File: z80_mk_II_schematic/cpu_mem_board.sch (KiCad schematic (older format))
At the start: 23 parts

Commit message: Lots more work on schematic
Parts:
- added C1, C3, C4: 0u1, symbol Device:C_Small
- added C2: 100u, symbol Device:CP_Small
- added J1: Conn_01x37_Male, symbol Connector:Conn_01x37_Male
- gave numbers to parts that had none: 23
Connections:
- net labels added: A0, A1, A10, A11, A12, A13, A2, A3, A4, A5, A6, A7, A8, A9, A[15..0], CPU_CLK, D0, D1, D2, D3, D4, D5, D6, D7, D[7..0], IO_CLK, IO_CLK_IN, NC, ~BUSAK~, ~BUSRQ~, ~EPROM_CE~, ~EXT_RESET~, ~INT~, ~IORQ~, ~M1~, ~MON_WR~, ~MREQ~, ~RAM0_CE~, ~RAM1_CE~, ~RD~, ~RESET_IN~, ~RESET~, ~WR~
- net labels removed: ~BUSAK, ~BUSRQ, ~CPU_CLK, ~CS_EPROM, ~CS_RAM0, ~CS_RAM1, ~INT, ~MON_WR, ~MREQ, ~RD, ~RESET
- wire segments 115 -> 251
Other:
- moved on the sheet: C5, D1, D2, Q1, Q2, Q3, R1, R10, R11, R2, R3, R4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

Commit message: Un-fsck something which made most of the chips into 74LS00 for some very odd reason. Also start to assign footprints.
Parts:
- R1, R10, R11, R2, R3, R4, R5, R6, R7, R8, R9: footprint (none) -> Resistors_ThroughHole:R_Axial_DIN0207_L6.3mm_D2.5mm_P10.16mm_Horizontal
- U1: footprint (none) -> Housings_DIP:DIP-40_W15.24mm_Socket
- U2, U3, U4: footprint Package_DIP:DIP-28_W15.24mm -> Housings_DIP:DIP-28_W15.24mm_Socket
- U5: footprint (none) -> Housings_DIP:DIP-16_W7.62mm_Socket
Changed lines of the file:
@@
 F 0 "R2" V 2300 1550 50  0000 C CNN
 F 1 "4K7" V 2100 1550 50  0000 C CNN
-F 2 "" H 2200 1550 50  0001 C CNN
+F 2 "Resistors_ThroughHole:R_Axial_DIN0207_L6.3mm_D2.5mm_P10.16mm_Horizontal" H 2200 1550 50  0001 C CNN
 F 3 "~" H 2200 1550 50  0001 C CNN
 	1    2200 1550
@@
 F 0 "R1" V 2100 1400 50  0000 C CNN
 F 1 "4K7" V 1900 1400 50  0000 C CNN
-F 2 "" H 2000 1400 50  0001 C CNN
+F 2 "Resistors_ThroughHole:R_Axial_DIN0207_L6.3mm_D2.5mm_P10.16mm_Horizontal" H 2000 1400 50  0001 C CNN
 F 3 "~" H 2000 1400 50  0001 C CNN
 	1    2000 1400
@@
 F 0 "R9" H 7509 5246 50  0000 L CNN
 F 1 "10K" H 7509 5155 50  0000 L CNN
-F 2 "" H 7450 5200 50  0001 C CNN
+F 2 "Resistors_ThroughHole:R_Axial_DIN0207_L6.3mm_D2.5mm_P10.16mm_Horizontal" H 7450 5200 50  0001 C CNN
 F 3 "~" H 7450 5200 50  0001 C CNN
 	1    7450 5200
@@
 F 0 "R8" V 7296 5450 50  0000 C CNN
 F 1 "10K" V 7205 5450 50  0000 C CNN
-F 2 "" H 7100 5450 50  0001 C CNN
+F 2 "Resistors_ThroughHole:R_Axial_DIN0207_L6.3mm_D2.5mm_P10.16mm_Horizontal" H 7100 5450 50  0001 C CNN
 F 3 "~" H 7100 5450 50  0001 C CNN
 	1    7100 5450
@@
 F 0 "R7" H 6841 4754 50  0000 R CNN
 F 1 "4K7" H 6841 4845 50  0000 R CNN
-F 2 "" H 6900 4800 50  0001 C CNN
+F 2 "Resistors_ThroughHole:R_Axial_DIN0207_L6.3mm_D2.5mm_P10.16mm_Horizontal" H 6900 4800 50  0001 C CNN
 F 3 "~" H 6900 4800 50  0001 C CNN
 	1    6900 4800
@@
 F 0 "R6" H 6491 4754 50  0000 R CNN
 F 1 "4K7" H 6491 4845 50  0000 R CNN
-F 2 "" H 6550 4800 50  0001 C CNN
+F 2 "Resistors_ThroughHole:R_Axial_DIN0207_L6.3mm_D2.5mm_P10.16mm_Horizontal" H 6550 4800 50  0001 C CNN
 F 3 "~" H 6550 4800 50  0001 C CNN
 	1    6550 4800
@@
 F 0 "R4" H 5742 1354 50  0000 R CNN
 F 1 "4K7" H 5742 1445 50  0000 R CNN
-F 2 "" H 5800 1400 50  0001 C CNN
+F 2 "Resistors_ThroughHole:R_Axial_DIN0207_L6.3mm_D2.5mm_P10.16mm_Horizontal" H 5800 1400 50  0001 C CNN
 F 3 "~" H 5800 1400 50  0001 C CNN
 	1    5800 1400
@@
 F 0 "U4" H 9050 2500 50  0000 C CNN
 F 1 "KM62256CLP" H 9050 2350 50  0000 C CNN
-F 2 "Package_DIP:DIP-28_W15.24mm" H 9050 2300 50  0001 C CNN
+F 2 "Housings_DIP:DIP-28_W15.24mm_Socket" H 9050 2300 50  0001 C CNN
 F 3 "https://www.futurlec.com/Datasheet/Memory/62256.pdf" H 9050 2300 50  0001 C CNN
 	1    9050 2400
@@
 F 0 "U3" H 7350 2500 50  0000 C CNN
 F 1 "27128" H 7350 2400 50  0000 C CNN
-F 2 "Package_DIP:DIP-28_W15.24mm" H 7300 2600 50  0001 C CNN
+F 2 "Housings_DIP:DIP-28_W15.24mm_Socket" H 7300 2600 50  0001 C CNN
 F 3 "http://eeshop.unl.edu/pdf/27128.pdf" H 7300 2600 50  0001 C CNN
 	1    7300 2600
@@
 F 0 "U2" H 5200 2450 50  0000 C CNN
 F 1 "KM62256CLP" H 5250 2300 50  0000 C CNN
-F 2 "Package_DIP:DIP-28_W15.24mm" H 5200 2300 50  0001 C CNN
+F 2 "Housings_DIP:DIP-28_W15.24mm_Socket" H 5200 2300 50  0001 C CNN
 F 3 "https://www.futurlec.com/Datasheet/Memory/62256.pdf" H 5200 2300 50  0001 C CNN
 	1    5200 2400
@@
 F 0 "U1" H 3050 3050 50  0000 C CNN
 F 1 "Z80CPU" H 3050 2850 50  0000 C CNN
-F 2 "" H 3050 3350 50  0001 C CNN
+F 2 "Housings_DIP:DIP-40_W15.24mm_Socket" H 3050 3350 50  0001 C CNN
 F 3 "www.zilog.com/manage_directlink.php?filepath=docs/z80/um0080" H 3050 3350 50  0001 C CNN
 	1    3050 2950
@@
 F 0 "R10" H 10209 4446 50  0000 L CNN
 F 1 "4K7" H 10209 4355 50  0000 L CNN
-F 2 "" H 10150 4400 50  0001 C CNN
+F 2 "Resistors_ThroughHole:R_Axial_DIN0207_L6.3mm_D2.5mm_P10.16mm_Horizontal" H 10150 4400 50  0001 C CNN
 F 3 "~" H 10150 4400 50  0001 C CNN
 	1    10150 4400
@@
 F 0 "R11" H 10459 4446 50  0000 L CNN
 F 1 "4K7" H 10459 4355 50  0000 L CNN
-F 2 "" H 10400 4400 50  0001 C CNN
+F 2 "Resistors_ThroughHole:R_Axial_DIN0207_L6.3mm_D2.5mm_P10.16mm_Horizontal" H 10400 4400 50  0001 C CNN
 F 3 "~" H 10400 4400 50  0001 C CNN
 	1    10400 4400
@@
 F 0 "U5" H 9250 5300 50  0000 C CNN
 F 1 "74LS156" H 9300 5150 50  0000 C CNN
-F 2 "" H 9250 5150 50  0001 C CNN
+F 2 "Housings_DIP:DIP-16_W7.62mm_Socket" H 9250 5150 50  0001 C CNN
 F 3 "http://www.ti.com/lit/gpn/sn74LS156" H 9250 5150 50  0001 C CNN
 	1    9250 5150
@@
 F 0 "R5" H 6191 2054 50  0000 R CNN
 F 1 "4K7" H 6191 2145 50  0000 R CNN
-F 2 "" H 6250 2100 50  0001 C CNN
+F 2 "Resistors_ThroughHole:R_Axial_DIN0207_L6.3mm_D2.5mm_P10.16mm_Horizontal" H 6250 2100 50  0001 C CNN
 F 3 "~" H 6250 2100 50  0001 C CNN
 	1    6250 2100
@@
 F 0 "R3" H 2191 4604 50  0000 R CNN
 F 1 "4K7" H 2191 4695 50  0000 R CNN
-F 2 "" H 2250 4650 50  0001 C CNN
+F 2 "Resistors_ThroughHole:R_Axial_DIN0207_L6.3mm_D2.5mm_P10.16mm_Horizontal" H 2250 4650 50  0001 C CNN
 F 3 "~" H 2250 4650 50  0001 C CNN
 	1    2250 4650

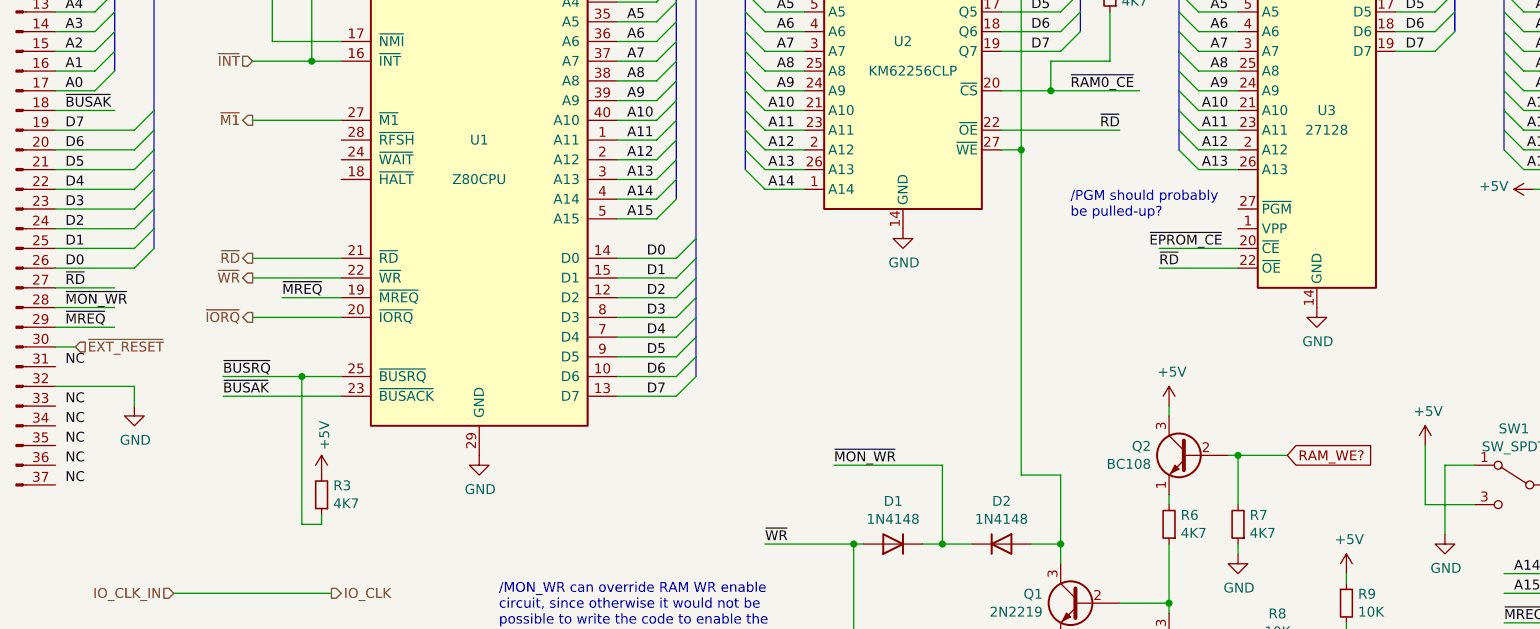
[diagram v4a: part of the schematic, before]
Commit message: Add some no-connection symbols.
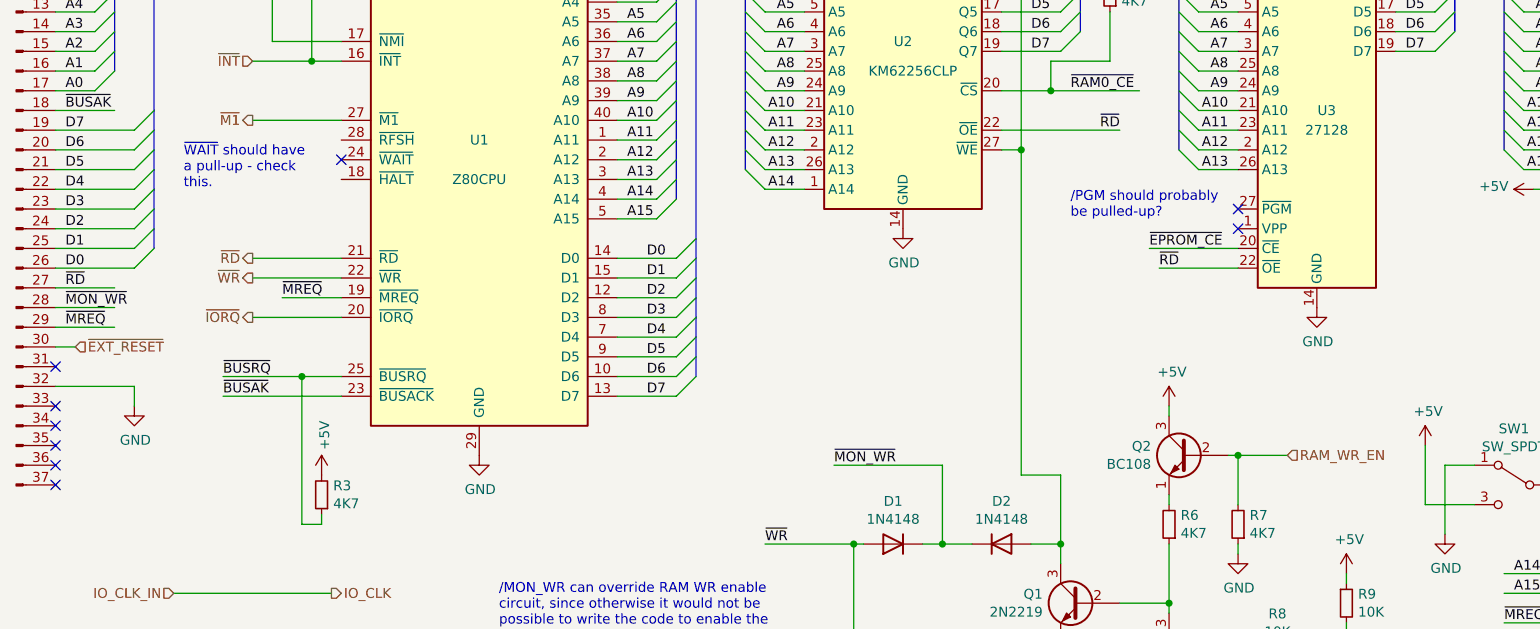
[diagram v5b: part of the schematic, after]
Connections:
- net labels added: RAM_WR_EN
- net labels removed: NC, RAM_WE?
- no-connect marks 0 -> 9
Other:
- note added: "~WAIT~ should have\na pull-up - check\nthis."
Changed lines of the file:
@@
 	0    -1   -1   0
 $EndComp
-Text GLabel 7150 4450 2    50   Input ~ 0
-RAM_WE?
 Connection ~ 6900 4450
 Wire Wire Line
@@
 Text Label 6450 3400 0    50   ~ 0
 ~EPROM_CE~
-Wire Wire Line
-	6500 3400 6900 3400
 Text Label 6050 2600 0    50   ~ 0
 ~RAM0_CE~
@@
 Text Label 950  3800 0    50   ~ 0
 ~MREQ~
-Text Label 950  4000 0    50   ~ 0
-NC
 $Comp
 L power:GND #PWR01
@@
 Text Label 900  1800 0    50   ~ 0
 ~BUSRQ~
-Text Label 950  4200 0    50   ~ 0
-NC
-Text Label 950  4300 0    50   ~ 0
-NC
-Text Label 950  4400 0    50   ~ 0
-NC
+Wire Wire Line
+	1500 5150 2300 5150
+Text HLabel 2300 5150 2    50   Output ~ 0
+IO_CLK
+Text HLabel 1500 5150 0    50   Input ~ 0
+IO_CLK_IN
+Text HLabel 1000 3900 2    50   Input ~ 0
+~EXT_RESET~
+Wire Wire Line
+	5800 1200 6250 1200
+Wire Wire Line
+	6250 1200 6250 2000
+Connection ~ 5800 1200
+$Comp
+L Device:C_Small C1
+U 1 1 60359873
+P 3000 6000
+F 0 "C1" V 2771 6000 50  0000 C CNN
+F 1 "0u1" V 2862 6000 50  0000 C CNN
+F 2 "" H 3000 6000 50  0001 C CNN
+F 3 "~" H 3000 6000 50  0001 C CNN
+	1    3000 6000
+	1    0    0    -1
+$EndComp
+$Comp
+L power:GND #PWR05
+U 1 1 6035A8B2
+P 3000 6100
+F 0 "#PWR05" H 3000 5850 50  0001 C CNN
+F 1 "GND" H 3005 5927 50  0000 C CNN
+F 2 "" H 3000 6100 50  0001 C CNN
+F 3 "" H 3000 6100 50  0001 C CNN
+	1    3000 6100
+	1    0    0    -1
+$EndComp
+$Comp
+L power:+5V #PWR04
+U 1 1 6035B940
+P 3000 5900
+F 0 "#PWR04" H 3000 5750 50  0001 C CNN
+F 1 "+5V" H 3015 6073 50  0000 C CNN
+F 2 "" H 3000 5900 50  0001 C CNN
+F 3 "" H 3000 5900 50  0001 C CNN
+	1    3000 5900
+	1    0    0    -1
+$EndComp
+$Comp
+L Device:C_Small C3
+U 1 1 6035ED0A
+P 3800 6000
+F 0 "C3" V 3571 6000 50  0000 C CNN
+F 1 "0u1" V 3662 6000 50  0000 C CNN
+F 2 "" H 3800 6000 50  0001 C CNN
+F 3 "~" H 3800 6000 50  0001 C CNN
+	1    3800 6000
+	1    0    0    -1
+$EndComp
+$Comp
+L power:GND #PWR011
+U 1 1 6035ED10
+P 3800 6100
+F 0 "#PWR011" H 3800 5850 50  0001 C CNN
+F 1 "GND" H 3805 5927 50  0000 C CNN
+F 2 "" H 3800 6100 50  0001 C CNN
+F 3 "" H 3800 6100 50  0001 C CNN
+	1    3800 6100
+	1    0    0    -1
+$EndComp
+$Comp
+L power:+5V #PWR010
+U 1 1 6035ED16
+P 3800 5900
+F 0 "#PWR010" H 3800 5750 50  0001 C CNN
+F 1 "+5V" H 3815 6073 50  0000 C CNN
+F 2 "" H 3800 5900 50  0001 C CNN
+F 3 "" H 3800 5900 50  0001 C CNN
+	1    3800 5900
+	1    0    0    -1
+$EndComp
+$Comp
+L Device:C_Small C4
+U 1 1 60379DCA
+P 4200 6000
+F 0 "C4" V 3971 6000 50  0000 C CNN
+F 1 "0u1" V 4062 6000 50  0000 C CNN
+F 2 "" H 4200 6000 50  0001 C CNN
+F 3 "~" H 4200 6000 50  0001 C CNN
+	1    4200 6000
+	1    0    0    -1
+$EndComp
+$Comp
+L power:GND #PWR013
+U 1 1 60379DD0
+P 4200 6100
+F 0 "#PWR013" H 4200 5850 50  0001 C CNN
+F 1 "GND" H 4205 5927 50  0000 C CNN
+F 2 "" H 4200 6100 50  0001 C CNN
+F 3 "" H 4200 6100 50  0001 C CNN
+	1    4200 6100
+	1    0    0    -1
+$EndComp
+$Comp
+L power:+5V #PWR012
+U 1 1 60379DD6
+P 4200 5900
+F 0 "#PWR012" H 4200 5750 50  0001 C CNN
+F 1 "+5V" H 4215 6073 50  0000 C CNN
+F 2 "" H 4200 5900 50  0001 C CNN
+F 3 "" H 4200 5900 50  0001 C CNN
+	1    4200 5900
+	1    0    0    -1
+$EndComp
+$Comp
+L power:GND #PWR09
+U 1 1 60395B39
+P 3400 6100
+F 0 "#PWR09" H 3400 5850 50  0001 C CNN
+F 1 "GND" H 3405 5927 50  0000 C CNN
+F 2 "" H 3400 6100 50  0001 C CNN
+F 3 "" H 3400 6100 50  0001 C CNN
+	1    3400 6100
+	1    0    0    -1
+$EndComp
+$Comp
+L power:+5V #PWR08
+U 1 1 60395B3F
+P 3400 5900
+F 0 "#PWR08" H 3400 5750 50  0001 C CNN
+F 1 "+5V" H 3415 6073 50  0000 C CNN
+F 2 "" H 3400 5900 50  0001 C CNN
+F 3 "" H 3400 5900 50  0001 C CNN
+	1    3400 5900
+	1    0    0    -1
+$EndComp
+$Comp
+L Device:CP_Small C2
+U 1 1 60593521
+P 3400 6000
+F 0 "C2" V 3150 5950 50  0000 L CNN
+F 1 "100u" V 3250 5900 50  0000 L CNN
+F 2 "" H 3400 6000 50  0001 C CNN
+F 3 "~" H 3400 6000 50  0001 C CNN
+	1    3400 6000
+	1    0    0    -1
+$EndComp
+Text HLabel 7150 4450 2    50   Input ~ 0
+RAM_WR_EN
+NoConn ~ 900  4200
+NoConn ~ 900  4300
+NoConn ~ 900  4400
+NoConn ~ 900  4500
+NoConn ~ 900  4600
+NoConn ~ 900  4000
 $Comp
 L Connector:Conn_01x37_Male J1
@@
 	1    0    0    -1
 $EndComp
-Text Label 950  4500 0    50   ~ 0
-NC
-Text Label 950  4600 0    50   ~ 0
-NC
-Wire Wire Line
-	1500 5150 2300 5150
-Text HLabel 2300 5150 2    50   Output ~ 0
-IO_CLK
-Text HLabel 1500 5150 0    50   Input ~ 0
-IO_CLK_IN
-Text HLabel 1000 3900 2    50   Input ~ 0
-~EXT_RESET~
-Wire Wire Line
-	5800 1200 6250 1200
-Wire Wire Line
-	6250 1200 6250 2000
-Connection ~ 5800 1200
-$Comp
-L Device:C_Small C1
-U 1 1 60359873
-P 3000 6000
-F 0 "C1" V 2771 6000 50  0000 C CNN
-F 1 "0u1" V 2862 6000 50  0000 C CNN
-F 2 "" H 3000 6000 50  0001 C CNN
-F 3 "~" H 3000 6000 50  0001 C CNN
-	1    3000 6000
-	1    0    0    -1
-$EndComp
-$Comp
-L power:GND #PWR05
-U 1 1 6035A8B2
-P 3000 6100
-F 0 "#PWR05" H 3000 5850 50  0001 C CNN
-F 1 "GND" H 3005 5927 50  0000 C CNN
-F 2 "" H 3000 6100 50  0001 C CNN
-F 3 "" H 3000 6100 50  0001 C CNN
-	1    3000 6100
-	1    0    0    -1
-$EndComp
-$Comp
-L power:+5V #PWR04
-U 1 1 6035B940
-P 3000 5900
-F 0 "#PWR04" H 3000 5750 50  0001 C CNN
-F 1 "+5V" H 3015 6073 50  0000 C CNN
-F 2 "" H 3000 5900 50  0001 C CNN
-F 3 "" H 3000 5900 50  0001 C CNN
-	1    3000 5900
-	1    0    0    -1
-$EndComp
-$Comp
-L Device:C_Small C3
-U 1 1 6035ED0A
-P 3800 6000
-F 0 "C3" V 3571 6000 50  0000 C CNN
-F 1 "0u1" V 3662 6000 50  0000 C CNN
-F 2 "" H 3800 6000 50  0001 C CNN
-F 3 "~" H 3800 6000 50  0001 C CNN
-	1    3800 6000
-	1    0    0    -1
-$EndComp
-$Comp
-L power:GND #PWR011
-U 1 1 6035ED10
-P 3800 6100
-F 0 "#PWR011" H 3800 5850 50  0001 C CNN
-F 1 "GND" H 3805 5927 50  0000 C CNN
-F 2 "" H 3800 6100 50  0001 C CNN
-F 3 "" H 3800 6100 50  0001 C CNN
-	1    3800 6100
-	1    0    0    -1
-$EndComp
-$Comp
-L power:+5V #PWR010
-U 1 1 6035ED16
-P 3800 5900
-F 0 "#PWR010" H 3800 5750 50  0001 C CNN
-F 1 "+5V" H 3815 6073 50  0000 C CNN
-F 2 "" H 3800 5900 50  0001 C CNN
-F 3 "" H 3800 5900 50  0001 C CNN
-	1    3800 5900
-	1    0    0    -1
-$EndComp
-$Comp
-L Device:C_Small C4
-U 1 1 60379DCA
-P 4200 6000
-F 0 "C4" V 3971 6000 50  0000 C CNN
-F 1 "0u1" V 4062 6000 50  0000 C CNN
-F 2 "" H 4200 6000 50  0001 C CNN
-F 3 "~" H 4200 6000 50  0001 C CNN
-	1    4200 6000
-	1    0    0    -1
-$EndComp
-$Comp
-L power:GND #PWR013
-U 1 1 60379DD0
-P 4200 6100
-F 0 "#PWR013" H 4200 5850 50  0001 C CNN
-F 1 "GND" H 4205 5927 50  0000 C CNN
-F 2 "" H 4200 6100 50  0001 C CNN
-F 3 "" H 4200 6100 50  0001 C CNN
-	1    4200 6100
-	1    0    0    -1
-$EndComp
-$Comp
-L power:+5V #PWR012
-U 1 1 60379DD6
-P 4200 5900
-F 0 "#PWR012" H 4200 5750 50  0001 C CNN
-F 1 "+5V" H 4215 6073 50  0000 C CNN
-F 2 "" H 4200 5900 50  0001 C CNN
-F 3 "" H 4200 5900 50  0001 C CNN
-	1    4200 5900
-	1    0    0    -1
-$EndComp
-$Comp
-L power:GND #PWR09
-U 1 1 60395B39
-P 3400 6100
-F 0 "#PWR09" H 3400 5850 50  0001 C CNN
-F 1 "GND" H 3405 5927 50  0000 C CNN
-F 2 "" H 3400 6100 50  0001 C CNN
-F 3 "" H 3400 6100 50  0001 C CNN
-	1    3400 6100
-	1    0    0    -1
-$EndComp
-$Comp
-L power:+5V #PWR08
-U 1 1 60395B3F
-P 3400 5900
-F 0 "#PWR08" H 3400 5750 50  0001 C CNN
-F 1 "+5V" H 3415 6073 50  0000 C CNN
-F 2 "" H 3400 5900 50  0001 C CNN
-F 3 "" H 3400 5900 50  0001 C CNN
-	1    3400 5900
-	1    0    0    -1
-$EndComp
-$Comp
-L Device:CP_Small C2
-U 1 1 60593521
-P 3400 6000
-F 0 "C2" V 3150 5950 50  0000 L CNN
-F 1 "100u" V 3250 5900 50  0000 L CNN
-F 2 "" H 3400 6000 50  0001 C CNN
-F 3 "~" H 3400 6000 50  0001 C CNN
-	1    3400 6000
-	1    0    0    -1
-$EndComp
+NoConn ~ 6900 3200
+NoConn ~ 6900 3300
+NoConn ~ 2350 2950
+Text Notes 1550 3100 0    50   ~ 0
+~WAIT~ should have\na pull-up - check\nthis.
+Wire Wire Line
+	6450 3400 6900 3400
 Wire Bus Line
 	1500 900  10450 900

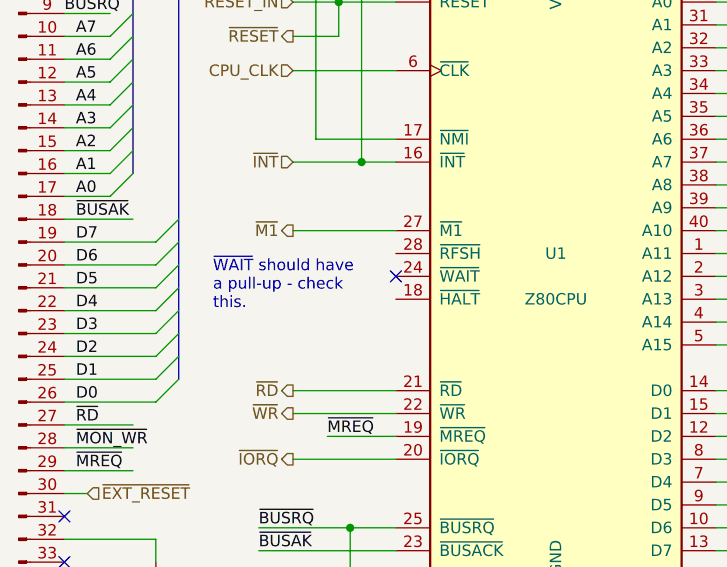
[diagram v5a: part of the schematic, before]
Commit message: Add missing connection for /wait.
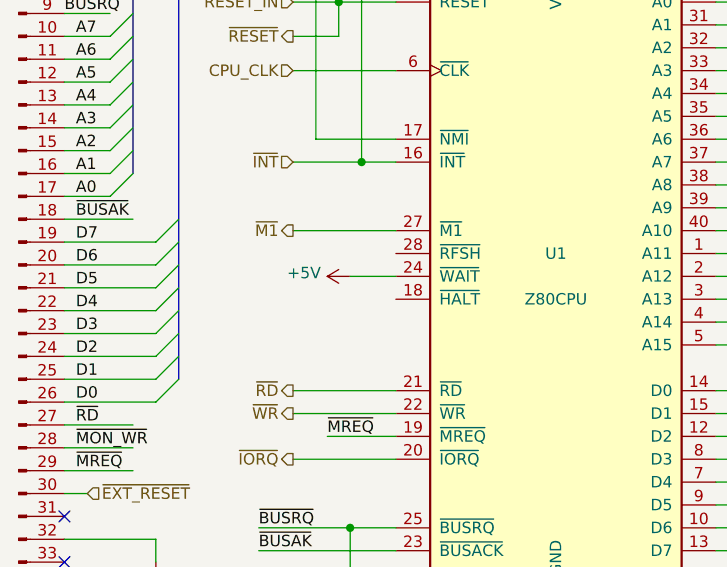
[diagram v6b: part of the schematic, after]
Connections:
- wire segments 251 -> 252
- no-connect marks 9 -> 8
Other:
- note removed: "~WAIT~ should have\na pull-up - check\nthis."
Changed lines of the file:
@@
 NoConn ~ 6900 3200
 NoConn ~ 6900 3300
-NoConn ~ 2350 2950
-Text Notes 1550 3100 0    50   ~ 0
-~WAIT~ should have\na pull-up - check\nthis.
 Wire Wire Line
 	6450 3400 6900 3400
+$Comp
+L power:+5V #PWR?
+U 1 1 5F9DDD0A
+P 2150 2950
+F 0 "#PWR?" H 2150 2800 50  0001 C CNN
+F 1 "+5V" V 2165 3078 50  0000 L CNN
+F 2 "" H 2150 2950 50  0001 C CNN
+F 3 "" H 2150 2950 50  0001 C CNN
+	1    2150 2950
+	0    -1   -1   0
+$EndComp
+Wire Wire Line
+	2350 2950 2150 2950
 Wire Bus Line
 	1500 900  10450 900
